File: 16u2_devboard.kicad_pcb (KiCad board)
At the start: 2 copper layers, 17.8 x 30.5 mm, 24 parts, among them J1 ISP, J2 USB_B_Micro, J3 CONN_L, J4 CONN_R, U1 ATmega16U2-M, Y1 16MHz

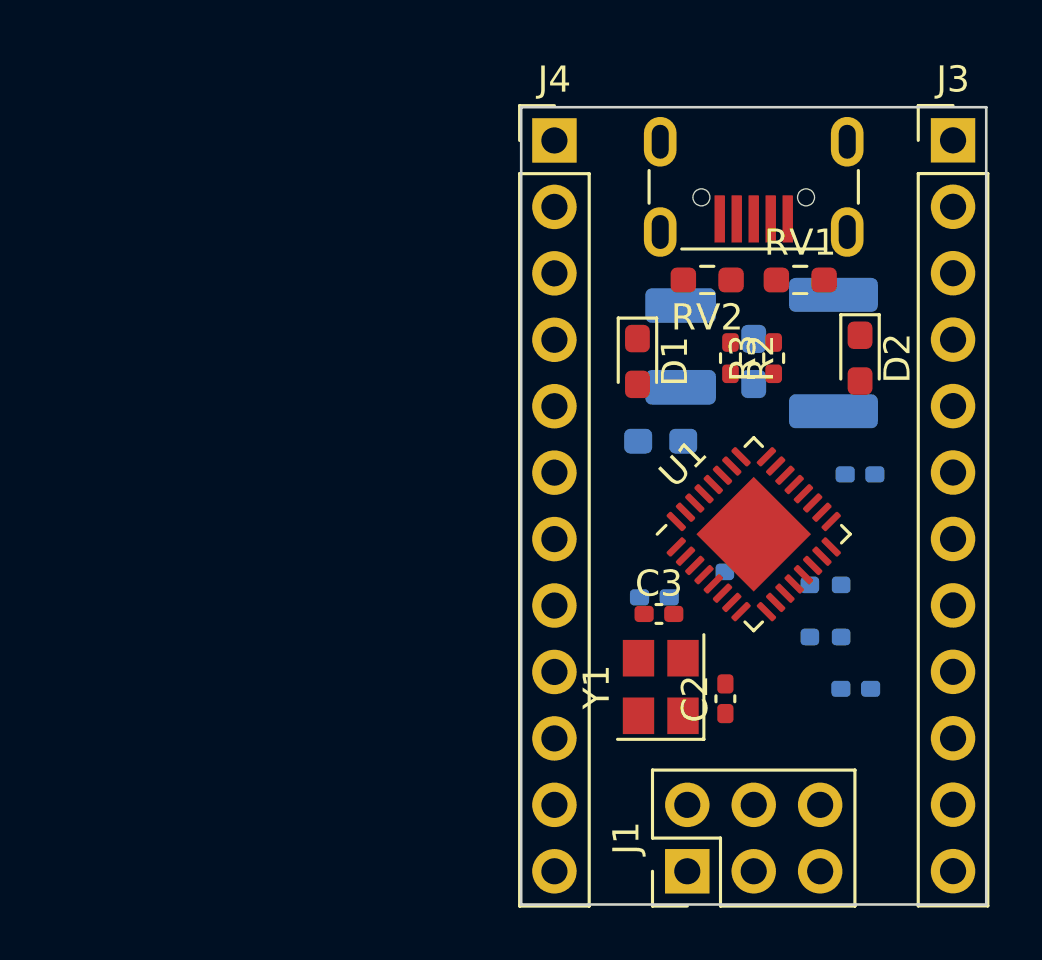
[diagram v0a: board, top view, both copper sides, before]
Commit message: Layout and routing in progress - removed most of front silkscreen
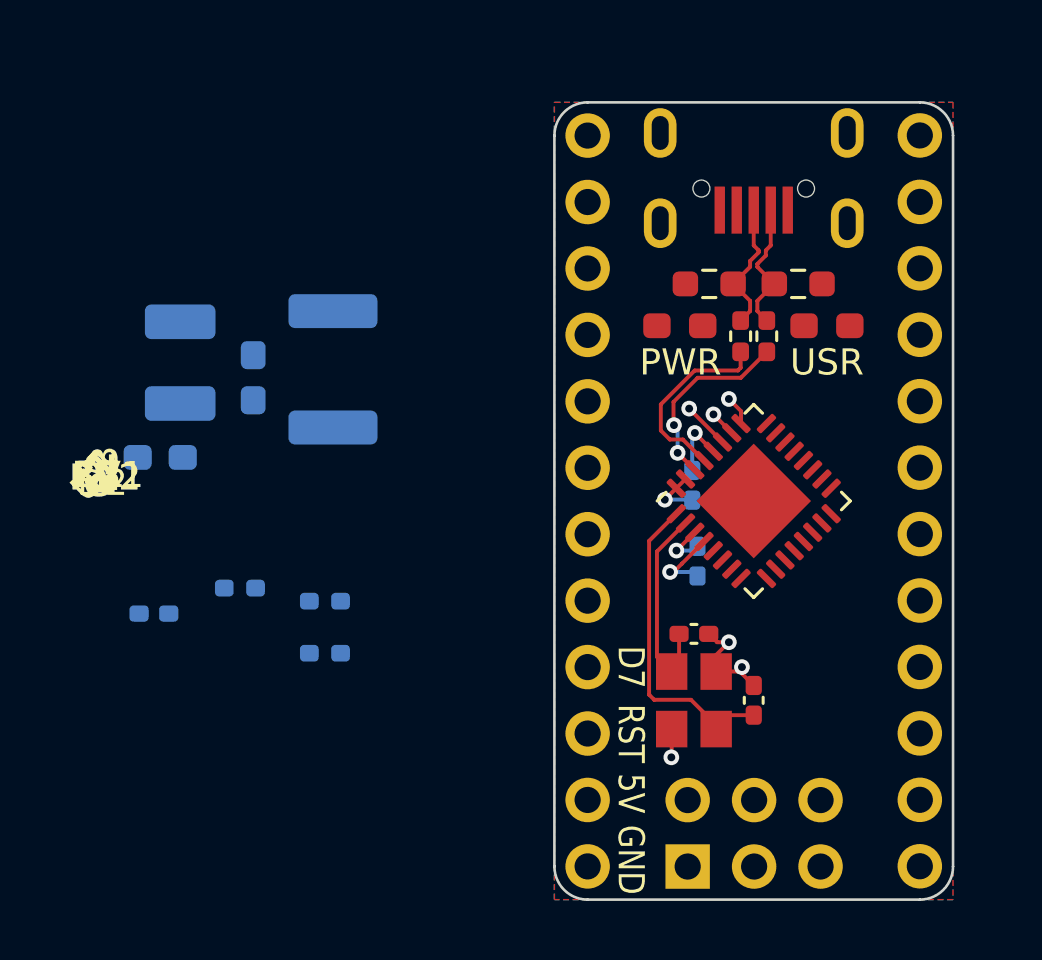
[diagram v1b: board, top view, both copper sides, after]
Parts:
- J3: moved to B.Cu
- Je: renamed from J4; moved to B.Cu
- moved R1 19.1 mm to (78.9, 66.6)
- moved C1 19.1 mm to (72.3, 65.1)
- moved C4 19.1 mm to (72.6, 59.1)
- moved C7 19.1 mm to (73.3, 55.5)
- moved C8 19.1 mm to (76.1, 56.1)
- moved F1 19.1 mm to (79.2, 55.7)
- moved R4 19.1 mm to (75.6, 64.1)
- moved R5 19.1 mm to (78.9, 64.6)
- moved C6 7.77 mm to (93.1, 63.1), turned to 90 degrees
- moved C5 6.43 mm to (92.9, 60.2), turned to 90 degrees
- moved D1 2.12 mm to (92.4, 54.1), turned to 180 degrees
- moved D2 1.77 mm to (98.0, 54.1), turned to 0 degrees
- moved C3 1.54 mm to (93.0, 65.9)
- moved Y1 1.37 mm to (93.0, 68.4)
- moved Je 1.28 mm to (88.9, 46.8), turned to 180 degrees
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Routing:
- net /XTAL1: track 0.00 -> 12.2 mm
- net GND: track 0.00 -> 9.60 mm, vias 0 -> 5
- net /XTAL2: track 0.00 -> 7.92 mm
- net D+: track 0.00 -> 7.37 mm
- net D-: track 0.00 -> 7.30 mm, vias 0 -> 2
- net /_D-: track 0.00 -> 5.12 mm
- net /_D+: track 0.00 -> 5.12 mm
- net +5V: track 0.00 -> 5.07 mm, vias 0 -> 2
- net /UCAP: track 0.00 -> 1.81 mm, vias 0 -> 1
- net PC5: track 0.00 -> 1.13 mm, vias 0 -> 1
- net PC4: track 0.00 -> 0.99 mm, vias 0 -> 1
- added copper zone on B.Cu, net GND
- added copper zone on F.Cu, net GND
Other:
- board size 17.8 x 30.5 mm -> 15.2 x 30.5 mm
- board text added: "5V"
- board text added: "D7"
- board text added: "GND"
- board text added: "PWR"
- board text added: "RST"
- board text added: "USR"

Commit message: v1.0 Finished - Layout and routing finished - Silkscreen markings added - Logo as part of ground pour
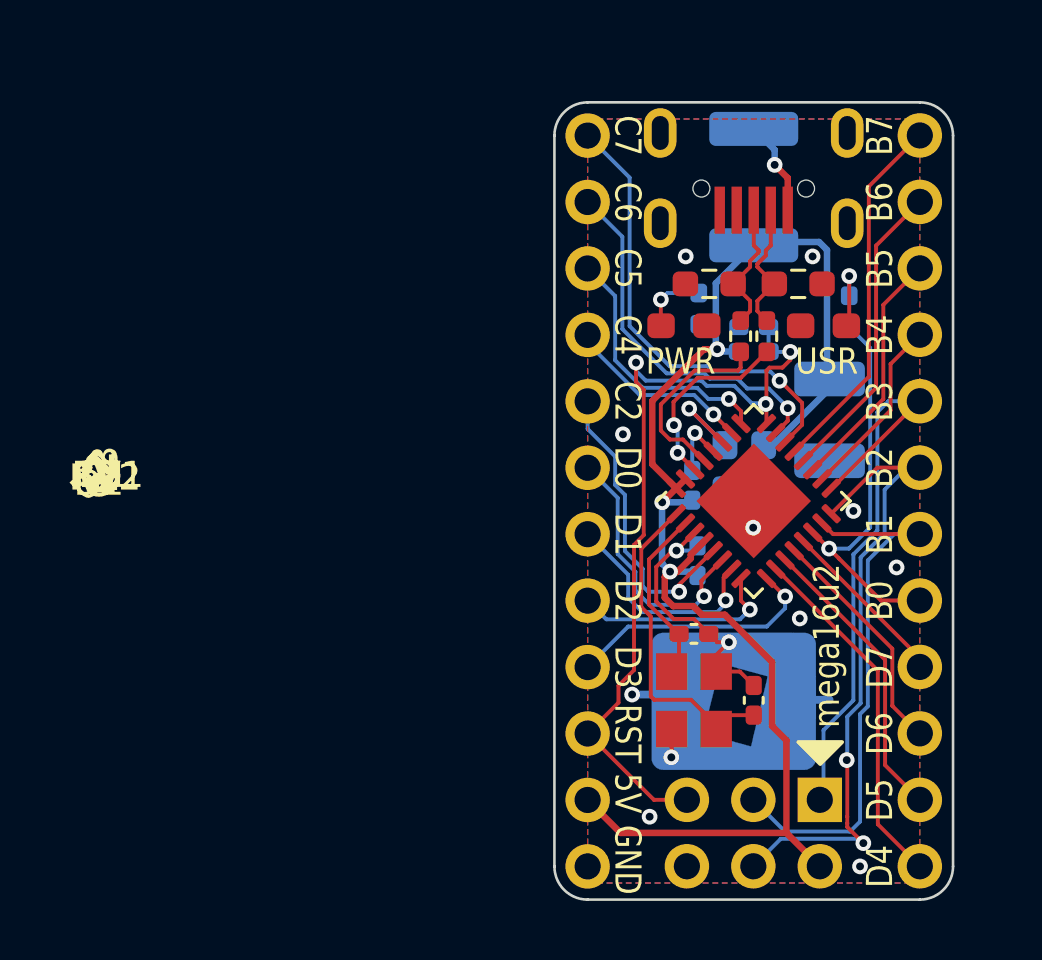
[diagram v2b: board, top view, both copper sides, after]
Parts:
- added TP1: LOGO, global:Logo_grounded, B.Cu at (94.5, 68.4)
- moved C1 25.4 mm to (95.2, 54.1), turned to 0 degrees
- moved C7 24.9 mm to (98.2, 57.7)
- moved R5 22.9 mm to (98.9, 53.5), turned to 90 degrees
- moved C4 21.6 mm to (94.2, 59.5), turned to -90 degrees
- moved R4 20.5 mm to (93.2, 53.4), turned to 90 degrees
- moved R1 20.0 mm to (95.2, 55.1), turned to 0 degrees
- moved C8 19.8 mm to (95.6, 59.5)
- moved F1 17.5 mm to (95.2, 48.8), turned to 90 degrees
- moved J1 5.66 mm to (97.8, 72.2), turned to -90 degrees
- moved D1 0.16 mm to (92.6, 54.1)
- moved D2 0.13 mm to (97.9, 54.1)
- renumbered Je to J4
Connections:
- J3 pad 1: PB0 -> PB7
- J3 pad 10: PC4 -> PD6
- J3 pad 11: PC5 -> PD5
- J3 pad 12: PC6 -> PD4
- J3 pad 2: PB1_SCK -> PB6
- J3 pad 3: PB2_MOSI -> PB5
- J3 pad 4: PB3_MISO -> PB4
- J3 pad 5: PB4 -> PB3_MISO
- J3 pad 6: PB5 -> PB2_MOSI
- J3 pad 7: PB6 -> PB1_SCK
- J3 pad 8: PB7 -> PB0_LED
- J3 pad 9: PC2 -> PD7
- J4 pad 2: PD0 -> PC6
- J4 pad 3: PD1 -> PC5
- J4 pad 4: PD2_TX -> PC4
- J4 pad 5: PD3_RX -> PC2
- J4 pad 6: PD4 -> PD0
- J4 pad 7: PD5 -> PD1
- J4 pad 8: PD6 -> PD2_TX
- J4 pad 9: PD7 -> PD3_RX
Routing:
- net +5V: track 5.07 -> 56.2 mm, vias 2 -> 3
- net RST: track 0.00 -> 31.0 mm, vias 0 -> 3
- net PB2_MOSI: track 0.00 -> 24.9 mm, vias 0 -> 2
- net PB3_MISO: track 0.00 -> 22.3 mm
- net PB1_SCK: track 0.00 -> 21.2 mm
- net PC7: track 0.00 -> 17.5 mm, vias 0 -> 1
- net GND: track 9.60 -> 25.1 mm, vias 5 -> 14
- net PB0_LED: track 0.00 -> 15.1 mm, vias 0 -> 1
- net PC6: track 0.00 -> 14.6 mm, vias 0 -> 1
- net PB7: track 0.00 -> 14.1 mm
- net PD4: track 0.00 -> 13.7 mm
- net PB6: track 0.00 -> 11.7 mm
- net PC2: track 0.00 -> 11.5 mm, vias 0 -> 1
- net PD5: track 0.00 -> 11.3 mm
- net PD0: track 0.00 -> 10.2 mm, vias 0 -> 1
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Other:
- board text added: "B0"
- board text added: "B1"
- board text added: "B2"
- board text added: "B3"
- board text added: "B4"
- board text added: "B5"
- board text added: "B6"
- board text added: "B7"
- board text added: "C2"
- board text added: "C4"
- board text added: "C5"
- board text added: "C6"
- board text added: "C7"
- board text added: "D0"
- board text added: "D1"
- board text added: "D2"
- board text added: "D3"
- board text added: "D4"
- board text added: "D5"
- board text added: "D6"
- board text added: "aspyra 2022"
- board text added: "mega16u2"
- board text added: "v1.0"

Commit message: Fix: Added JLC order number placeholder
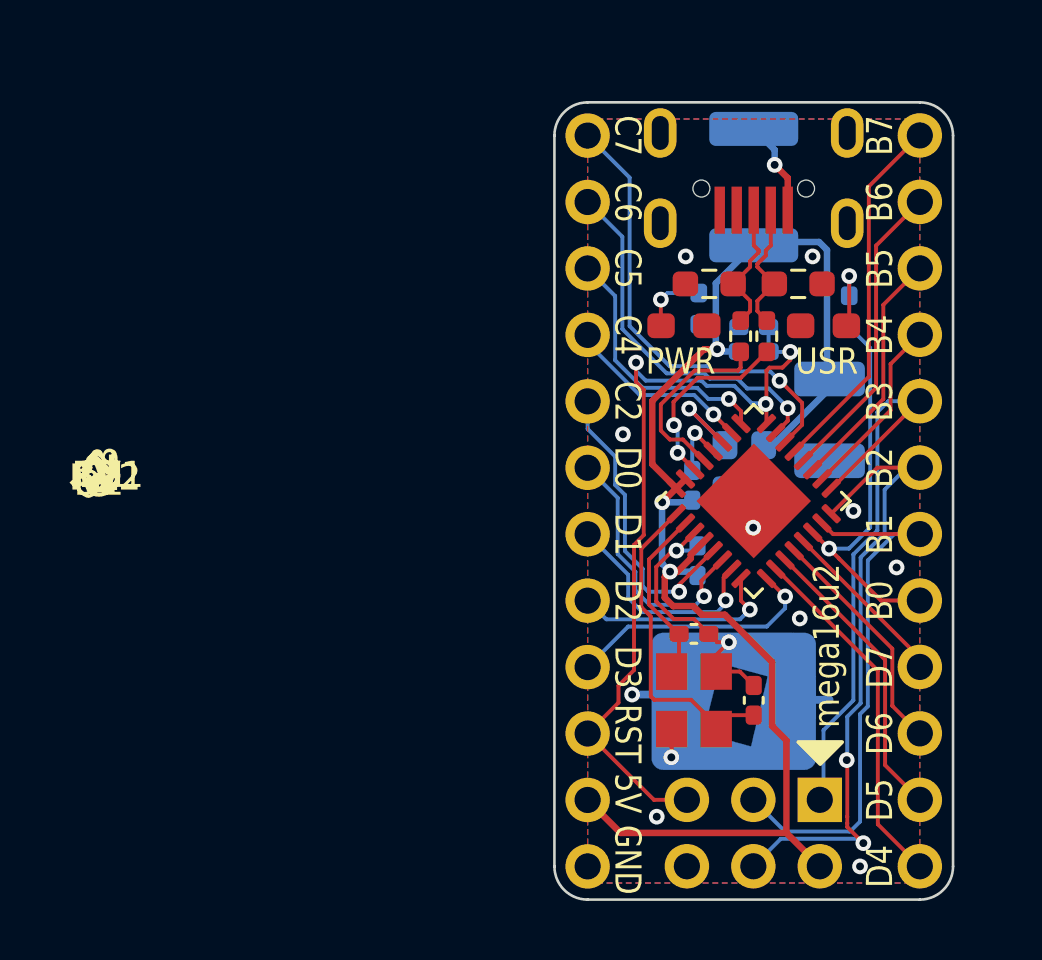
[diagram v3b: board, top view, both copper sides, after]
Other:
- board text added: "JLCJLCJLCJLC"
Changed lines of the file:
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@@
     (fp_line (start 1.6 -1.25) (end -1.6 -1.25) (layer "B.Fab") (width 0.1))
     (fp_line (start 1.6 1.25) (end 1.6 -1.25) (layer "B.Fab") (width 0.1))
-    (pad "1" smd roundrect (at -1.5625 0 270) (size 1.325 2.7) (layers "B.Cu" "B.Paste" "B.Mask") (roundrect_rratio 0.188679)
-      (net 3 "+5V") (pintype "passive"))
-    (pad "2" smd roundrect (at 1.5625 0 270) (size 1.325 2.7) (layers "B.Cu" "B.Paste" "B.Mask") (roundrect_rratio 0.188679)
+    (pad "1" smd roundrect (at -1.5625 0 270) (size 1.325 2.7) (layers "B.Cu" "B.Paste" "B.Mask") (roundrect_rratio 0.1886792453)
+      (net 3 "+5V") (pintype "passive"))
+    (pad "2" smd roundrect (at 1.5625 0 270) (size 1.325 2.7) (layers "B.Cu" "B.Paste" "B.Mask") (roundrect_rratio 0.1886792453)
       (net 1 "GND") (pintype "passive"))
     (model "${KICAD6_3DMODEL_DIR}/Capacitor_SMD.3dshapes/C_1210_3225Metric.wrl"
@@
     (fp_line (start 2.25 1.6) (end 2.25 -1.6) (layer "B.Fab") (width 0.1))
     (fp_line (start -2.25 -1.6) (end -2.25 1.6) (layer "B.Fab") (width 0.1))
-    (pad "1" smd roundrect (at -2.225 0 90) (size 1.3 3.4) (layers "B.Cu" "B.Paste" "B.Mask") (roundrect_rratio 0.192308)
-      (net 3 "+5V") (pintype "passive"))
-    (pad "2" smd roundrect (at 2.225 0 90) (size 1.3 3.4) (layers "B.Cu" "B.Paste" "B.Mask") (roundrect_rratio 0.192308)
+    (pad "1" smd roundrect (at -2.225 0 90) (size 1.3 3.4) (layers "B.Cu" "B.Paste" "B.Mask") (roundrect_rratio 0.1923076923)
+      (net 3 "+5V") (pintype "passive"))
+    (pad "2" smd roundrect (at 2.225 0 90) (size 1.3 3.4) (layers "B.Cu" "B.Paste" "B.Mask") (roundrect_rratio 0.1923076923)
       (net 34 "/5V_USB") (pintype "passive"))
     (model "${KICAD6_3DMODEL_DIR}/Fuse.3dshapes/Fuse_1812_4532Metric.wrl"
@@
   (gr_text "v1.0" (at 97.9 64.52336 90) (layer "B.SilkS")
     (effects (font (size 1 0.85) (thickness 0.153)) (justify mirror))
+  )
+  (gr_text "JLCJLCJLCJLC" (at 90.6272 69.96816 90) (layer "B.SilkS")
+    (effects (font (size 1 1) (thickness 0.153)) (justify mirror))
   )
   (gr_text "B6" (at 100.076 49.34336 90) (layer "F.SilkS")
@@
   (segment (start 92.146524 62.669091) (end 91.521969 63.293646) (width 0.15) (layer "F.Cu") (net 1))
   (segment (start 92.996097 61.968725) (end 92.295731 62.669091) (width 0.15) (layer "F.Cu") (net 1))
-  (via (at 91.27 72.84336) (size 0.6) (drill 0.3) (layers "F.Cu" "B.Cu") (free) (net 1))
+  (via (at 91.5416 72.84336) (size 0.6) (drill 0.3) (layers "F.Cu" "B.Cu") (free) (net 1))
   (via (at 94.3 66.17336) (size 0.6) (drill 0.3) (layers "F.Cu" "B.Cu") (net 1))
   (via (at 90.6 68.17336) (size 0.6) (drill 0.3) (layers "F.Cu" "B.Cu") (free) (net 1))
